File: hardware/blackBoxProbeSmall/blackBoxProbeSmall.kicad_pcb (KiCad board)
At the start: 4 copper layers, 44 x 29 mm, 79 parts, among them J1 USB-ID, J2 JTAG_2X05, J3 JTAG_2X05, J4 DevBoardUartInput, Q1 Q_NMOS_DUAL, Q2 Q_PMOS_DUAL, U1 MCP1702-MB, U2 USBLC6-2, U3 STM32F103CBT, U4 74X2T45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

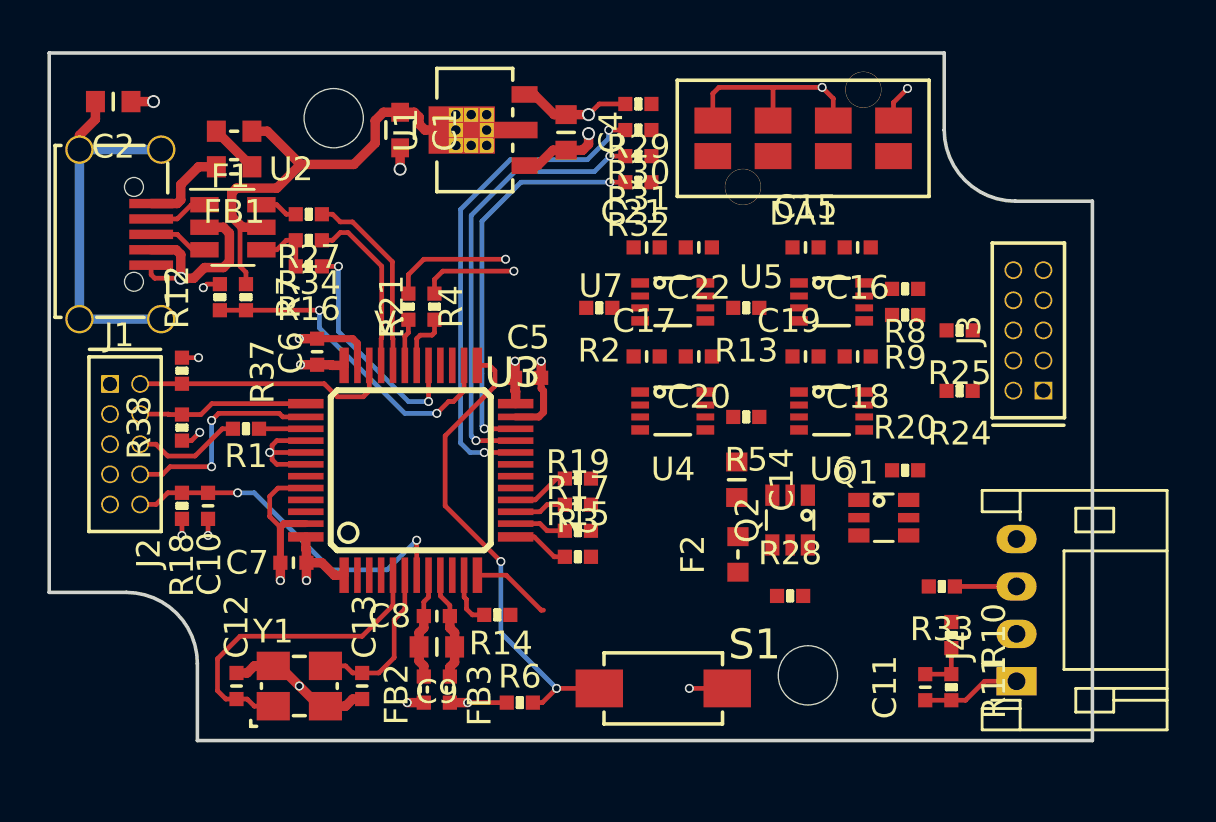
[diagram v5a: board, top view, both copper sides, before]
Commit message: compacted microcontroller area more
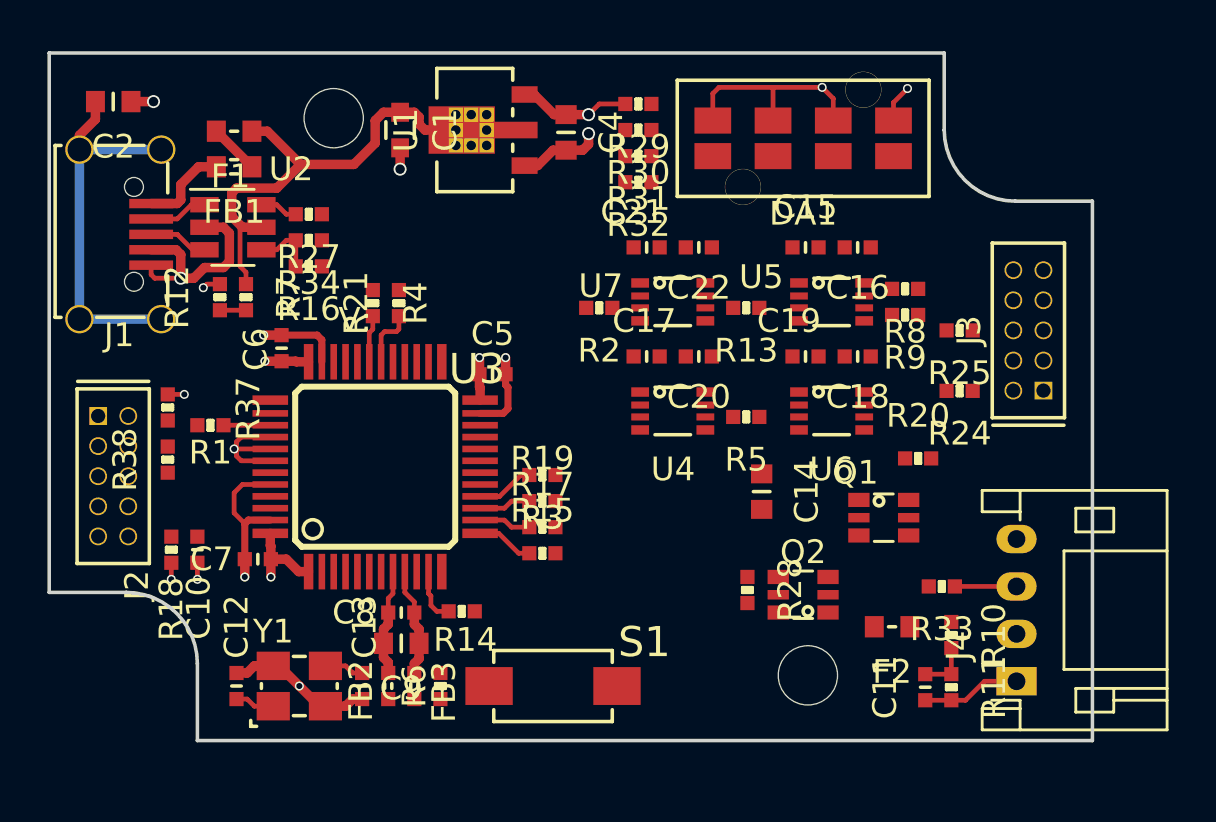
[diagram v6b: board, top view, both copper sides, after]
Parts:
- moved F2 7.18 mm to (159.2, 109.1), turned to 180 degrees
- moved S1 4.65 mm to (144.9, 111.6)
- moved R6 3.42 mm to (140.2, 111.6), turned to 90 degrees
- moved Q2 3.20 mm to (155.5, 107.8), turned to 90 degrees
- moved C10 1.90 mm to (129.9, 105.8)
- moved R18 1.90 mm to (128.8, 105.8)
- moved R28 1.82 mm to (153.2, 107.5), turned to 270 degrees
- moved R37 1.66 mm to (128.7, 99.8)
- moved C6 1.51 mm to (133.5, 97.3)
- moved C7 1.51 mm to (132.5, 106.2)
- moved C8 1.51 mm to (138.6, 108.5)
- moved C9 1.51 mm to (138.6, 109.8)
- moved FB2 1.51 mm to (138.0, 111.6)
- moved FB3 1.51 mm to (139.1, 111.6)
- moved N2 1.51 mm to (141.5, 96.2)
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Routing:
- net /LED0: track 20.9 -> 0.00 mm, vias 2 -> 0
- net /BUTTON: track 20.1 -> 0.00 mm, vias 2 -> 0
- net /LED1: track 18.8 -> 0.00 mm, vias 2 -> 0
- net /LED2: track 16.8 -> 0.00 mm, vias 2 -> 0
- net /MCU_RST: track 15.2 -> 0.00 mm, vias 2 -> 0
- net /USB_V: track 14.0 -> 1.10 mm, vias 2 -> 0
- net Net-(C12-Pad1): track 13.6 -> 1.67 mm
- net /MCU_TMS: track 11.1 -> 0.00 mm
- net /USB_PU: track 10.00 -> 0.00 mm, vias 2 -> 0
- net /MCU_TDI: track 9.26 -> 0.00 mm, vias 2 -> 0
- net /USB_D-: track 8.18 -> 0.00 mm
- net /USB_D+: track 7.44 -> 0.00 mm
- net /MCU_TCK: track 7.19 -> 0.00 mm
- net Net-(C13-Pad1): track 6.95 -> 1.67 mm
- net Net-(R4-Pad1): track 5.17 -> 0.00 mm, vias 1 -> 0
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
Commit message: removed last references of PROBE_E_VDD
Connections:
- C16 pad 1: /PROBE_E_VDD -> /PROBE_VDD
- C18 pad 1: /PROBE_E_VDD -> /PROBE_VDD
- C20 pad 1: /PROBE_E_VDD -> /PROBE_VDD
- C22 pad 1: /PROBE_E_VDD -> /PROBE_VDD
- R20 pad 1: /PROBE_E_VDD -> /PROBE_VDD

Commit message: further layout
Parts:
- moved R20 6.22 mm to (155.8, 106.3), turned to 90 degrees
- moved Q2 4.99 mm to (152.1, 111.4)
- moved R28 4.99 mm to (149.8, 111.2)
- moved F2 4.12 mm to (155.2, 108.3)
- moved Q1 1.75 mm to (158.2, 106.1), turned to 90 degrees
- moved R1 1.23 mm to (130.8, 101.8), turned to 90 degrees
- moved R10 0.78 mm to (161.2, 110.0), turned to 0 degrees
- moved R21 0.25 mm to (138.7, 95.5)
- moved R4 0.25 mm to (137.6, 95.5)
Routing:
- net /BUTTON: track 0.00 -> 17.3 mm
- net /MCU_TMS: track 0.00 -> 11.0 mm
- net Net-(C12-Pad1): track 1.67 -> 12.5 mm
- net /MCU_TDI: track 0.00 -> 8.99 mm
- net /USB_D-: track 0.00 -> 8.11 mm
- net /USB_D+: track 0.00 -> 7.36 mm
- net /MCU_TCK: track 0.00 -> 7.22 mm
- net /MCU_TDO: track 0.00 -> 5.86 mm
- net Net-(C13-Pad1): track 1.67 -> 6.91 mm
- net /VDD: track 18.6 -> 22.4 mm, vias 7 -> 8
- net Net-(R1-Pad1): track 1.97 -> 3.76 mm
- net /VSS: track 49.9 -> 51.4 mm, vias 12 -> 14
